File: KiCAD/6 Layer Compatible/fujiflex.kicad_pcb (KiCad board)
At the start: 2 copper layers, 27.7 x 43.7 mm, 33 parts, among them J1 505278-1933, U1 XC3S200A-4VQG100C, U2 AT25SF041B-MAHD-T, U3 AP2127N-1.2

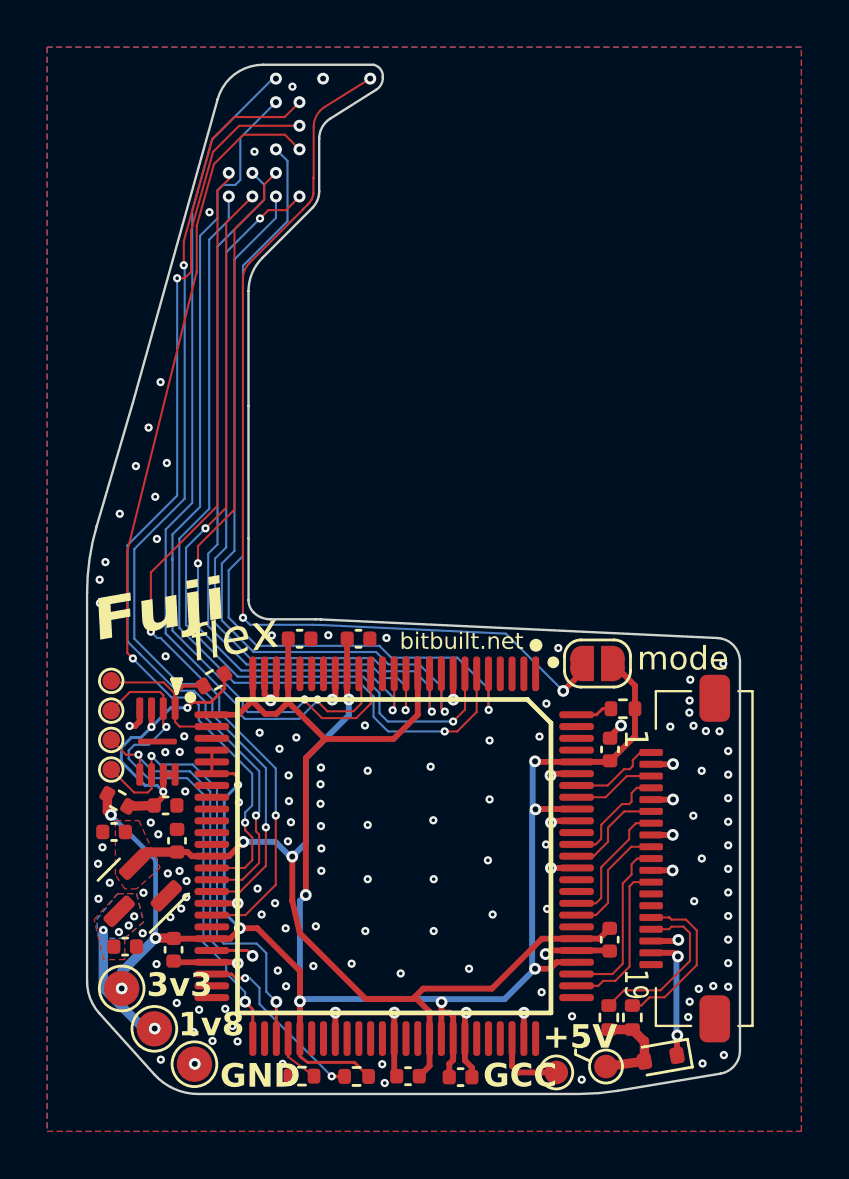
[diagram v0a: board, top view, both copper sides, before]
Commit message: minor layout updates
-updated grounding and some via sizes
-fixed IR button on 6L version
-updated gerbers
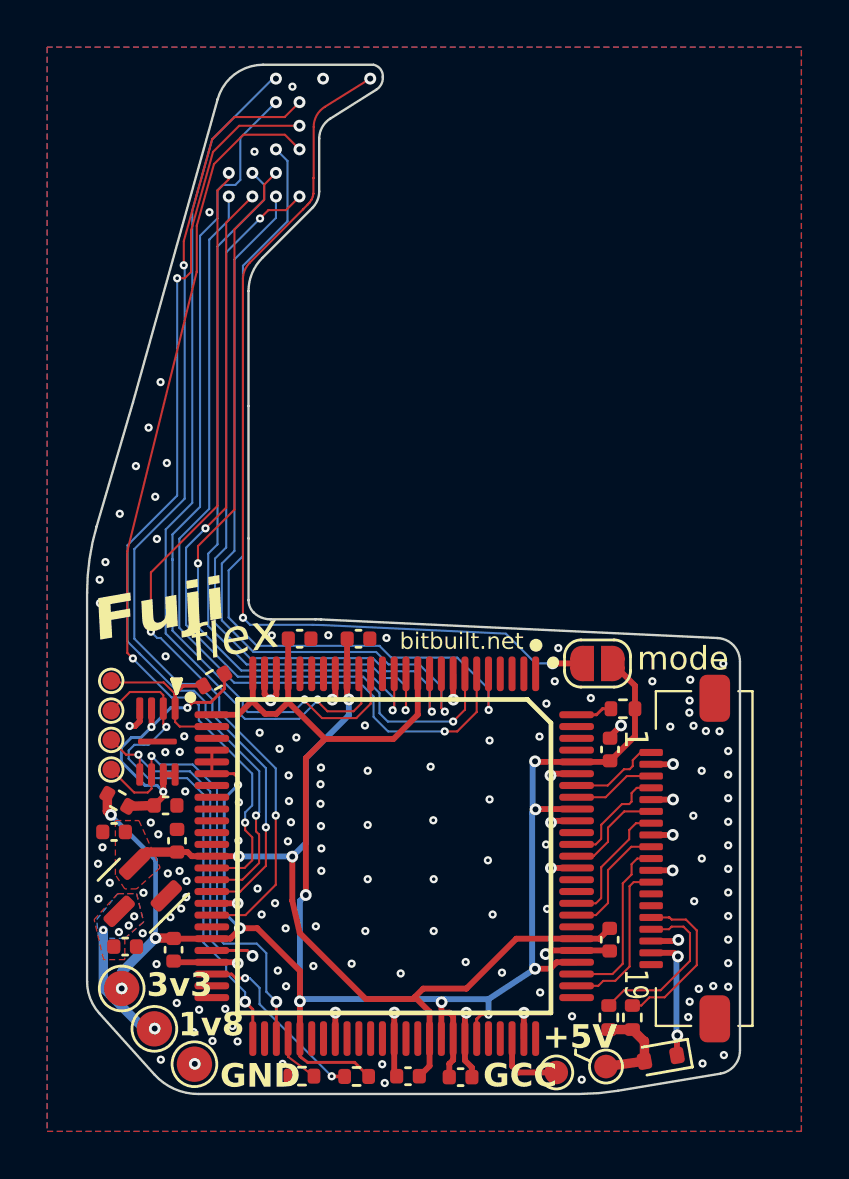
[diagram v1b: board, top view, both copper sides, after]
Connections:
- U1 pad 70: unconnected-(U1-IO_L05P_1-Pad70) -> +3.3V
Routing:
- net +3.3V: track 96.6 -> 98.5 mm, vias 11 -> 12
- net MODE: track 41.5 -> 40.3 mm
- net +1V2: track 40.4 -> 39.9 mm
- net GND: vias 144 -> 149
